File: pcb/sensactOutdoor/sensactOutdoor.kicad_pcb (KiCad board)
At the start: 2 copper layers, 100 x 81 mm, 126 parts, among them J1 48V, J10 CAN, J11 EXT2, J12 OW, J13 RGB, J14 CAN, J15 PWM_OUT, J16 24V, J2 Conn_01x03, J3 Conn_01x03, J4 PROG, J5 LED CC, J7 EXT1, J8 PWM_OUT, J9 230V, K1 ALDP105W, K2 ALDP105W, K3 ALDP105W, K4 ALDP105W, K5 ALDP105W, K6 ALDP105W, M1 BxxyyS-1WR, Q1 N, Q10 BC847, Q11 BC847, Q2 N, Q3 N, Q4 N, Q5 N, Q6 BC847, Q7 BC847, Q8 BC847, Q9 BC847, SW1 TERM OFF ON, SW2 RESET, U1 ESP32-WROOM-32U, U2 A6211, U3 LM2596Board, U4 ISO1050DUB, U5 AMS1117-3.3, U6 RF, U7 RX470B, U8 EL817

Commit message: Various PCB Updates
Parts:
- removed D7: LK1, LED_SMD:LED_0805_2012Metric_Pad1.15x1.40mm_HandSolder
- removed R34: k22, Resistor_SMD:R_0805_2012Metric_Pad1.20x1.40mm_HandSolder
- added D10: D, liebler_SEMICONDUCTORS:D_SOD-123_handsolder, B.Cu at (93.2, 25.1)
- added D11: D, liebler_SEMICONDUCTORS:D_SOD-123_handsolder, B.Cu at (93.1, 33.0)
- added D12: D, liebler_SEMICONDUCTORS:D_SOD-123_handsolder, B.Cu at (93.0, 45.2)
- added D13: D, liebler_SEMICONDUCTORS:D_SOD-123_handsolder, B.Cu at (93.0, 51.1)
- added D14: D, liebler_SEMICONDUCTORS:D_SOD-123_handsolder, B.Cu at (93.2, 59.1)
- added D15: D, liebler_SEMICONDUCTORS:D_SOD-123_handsolder, B.Cu at (93.2, 68.6)
- added U9: MAX98357_MODULE, Connector_PinHeader_2.54mm:PinHeader_1x07_P2.54mm_Vertical, F.Cu at (81.4, 43.3)
- moved R24 9.46 mm to (90.6, 56.8), turned to 270 degrees
- moved R5 7.53 mm to (84.6, 28.3)
- moved Q7 7.15 mm to (85.9, 34.2), turned to 270 degrees
- moved R23 5.81 mm to (87.2, 51.1), turned to 180 degrees
- moved Q10 5.39 mm to (86.6, 54.9), turned to 270 degrees
- moved R6 5.27 mm to (83.1, 33.5), turned to 270 degrees
- moved Q11 5.23 mm to (87.6, 60.5), turned to 270 degrees
- moved Q6 4.83 mm to (89.3, 27.6)
- moved R27 0.76 mm to (82.3, 61.7)
- moved C11 0.51 mm to (77.1, 58.2)
- moved C24 0.51 mm to (77.1, 60.6)
- moved C25 0.51 mm to (77.1, 63.1)
- moved D9 0.46 mm to (42.1, 33.0)
- moved U4 0.08 mm to (39.2, 65.5)
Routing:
- net +5V: track 155.0 -> 177.0 mm
- net +3V3: track 159.5 -> 170.8 mm, vias 3 -> 5
- net Net-(D12-Pad2): track 2.57 -> 13.4 mm
- net Net-(D14-Pad2): track 2.62 -> 12.0 mm
- net K1: track 28.2 -> 19.2 mm
- net Net-(D15-Pad2): track 2.88 -> 11.6 mm
- net Net-(D11-Pad2): track 2.99 -> 11.4 mm
- net Net-(D7-Pad2): track 8.22 -> 0.00 mm, vias 1 -> 0
- net Net-(D10-Pad2): track 1.87 -> 7.47 mm
- net K5: track 46.2 -> 41.3 mm
- net K2: track 22.2 -> 18.6 mm
- net Net-(Q11-Pad1): track 2.45 -> 4.60 mm
- net GND: track 117.5 -> 119.2 mm, vias 18 -> 17
- net SDA: track 28.5 -> 29.8 mm
- net K6: track 54.5 -> 53.3 mm
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
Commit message: Updated sensactHsNano
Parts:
- added JP3: 5Vx, Connector_PinHeader_2.54mm:PinHeader_1x02_P2.54mm_Vertical, F.Cu at (79.2, 69.9)
- D10, D11, D12, D13, D14, D15: value D -> 1N4148
- moved C5 21.1 mm to (61.1, 77.3), turned to 0 degrees
- moved C7 13.0 mm to (64.5, 66.5)
- moved C9 12.9 mm to (62.2, 66.5)
- moved C21 0.13 mm to (61.1, 74.9)
- moved C20 0.06 mm to (61.1, 72.6)
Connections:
- PS1 pad 4: +5V -> Net-(JP3-Pad1)
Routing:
- net +5V: track 177.0 -> 166.8 mm
- net Net-(JP3-Pad1): track 0.00 -> 4.66 mm
- net GND: track 119.2 -> 123.1 mm

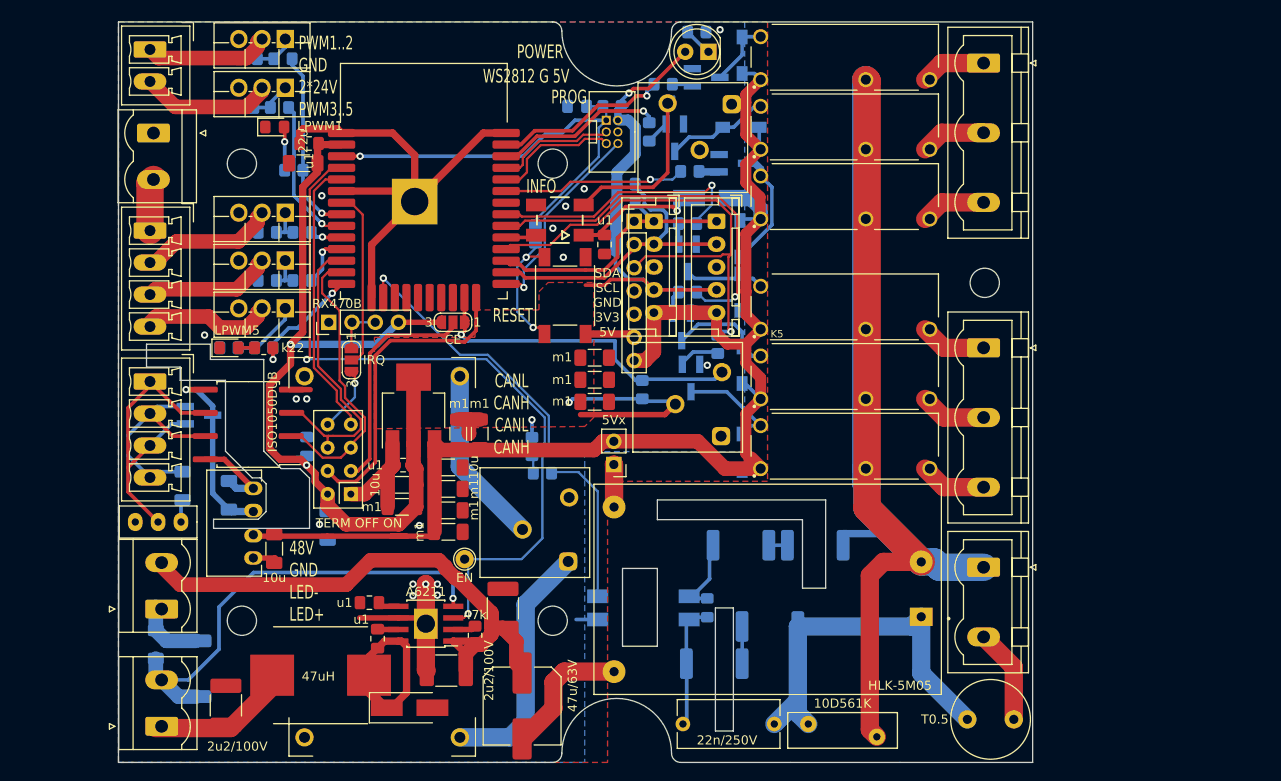
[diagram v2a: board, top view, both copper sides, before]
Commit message: sensactUP2, sensactHsNano sensactHsLED sensactOutdoor as ordered at JLCPCB
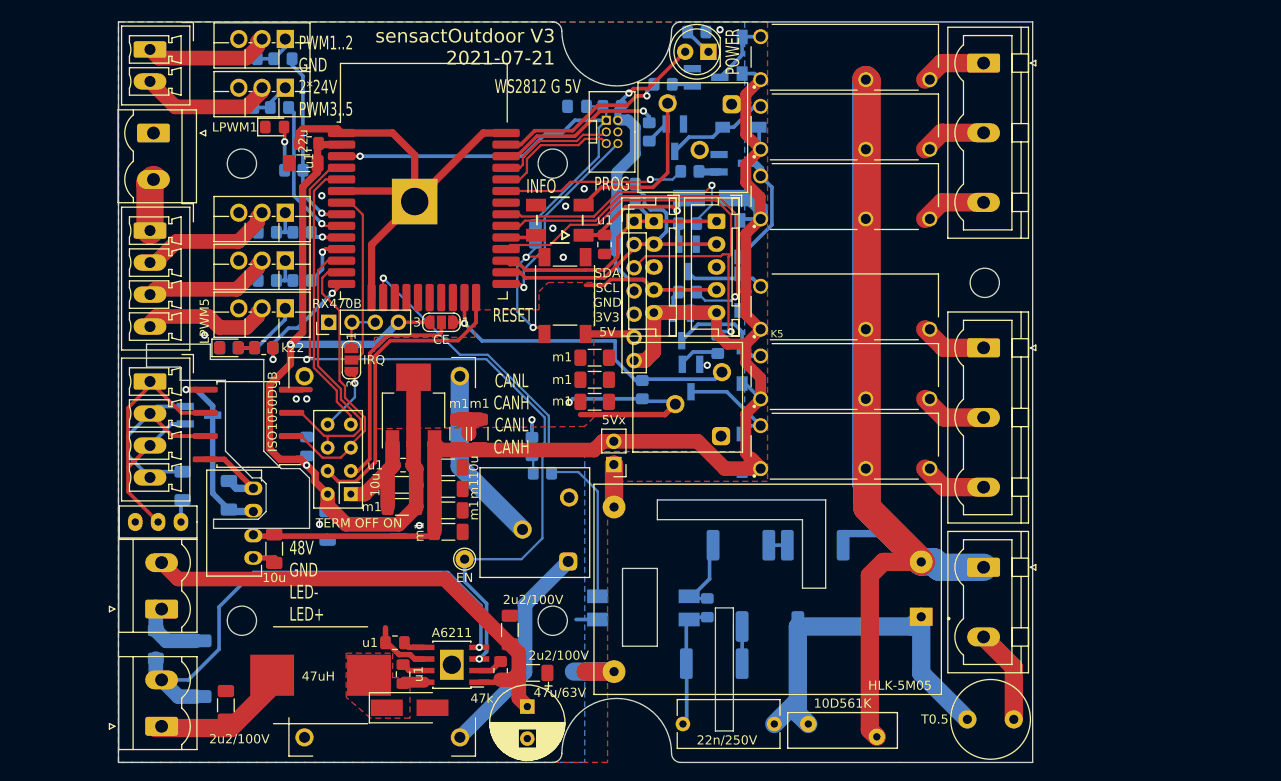
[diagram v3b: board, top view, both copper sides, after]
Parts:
- C1: footprint Capacitor_SMD:C_Elec_8x10.2 -> Capacitor_THT:CP_Radial_D8.0mm_P3.50mm
- C10, C2, C4: footprint Capacitor_SMD:C_1812_4532Metric_Pad1.57x3.40mm_HandSolder -> Capacitor_SMD:C_1206_3216Metric_Pad1.33x1.80mm_HandSolder
- moved C4 8.26 mm to (67.8, 88.0), turned to 90 degrees
- moved C2 7.80 mm to (70.4, 92.7), turned to 0 degrees
- moved U2 5.32 mm to (61.5, 91.8)
- moved C6 5.20 mm to (55.2, 89.4)
- moved C8 4.78 mm to (56.1, 92.8)
- moved R1 4.77 mm to (66.8, 92.5)
- moved JP1 1.27 mm to (60.3, 54.4)
- moved C1 0.58 mm to (69.7, 96.4)
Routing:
- net GND: track 123.1 -> 105.4 mm, vias 17 -> 12
- net /LED_SW: track 19.6 -> 2.40 mm
- net /LED_CC-: track 49.7 -> 55.8 mm
- net +48V: track 59.7 -> 54.2 mm
- net LED_CC_EN: track 57.6 -> 61.9 mm
- net /OUT+: track 27.4 -> 24.1 mm
- net +3V3: track 170.8 -> 169.5 mm
- net CE: track 25.0 -> 24.1 mm
- net CSN: track 34.1 -> 33.5 mm
- net OneWire: track 36.4 -> 37.0 mm
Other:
- board text added: "sensactOutdoor V3 2021-07-21"

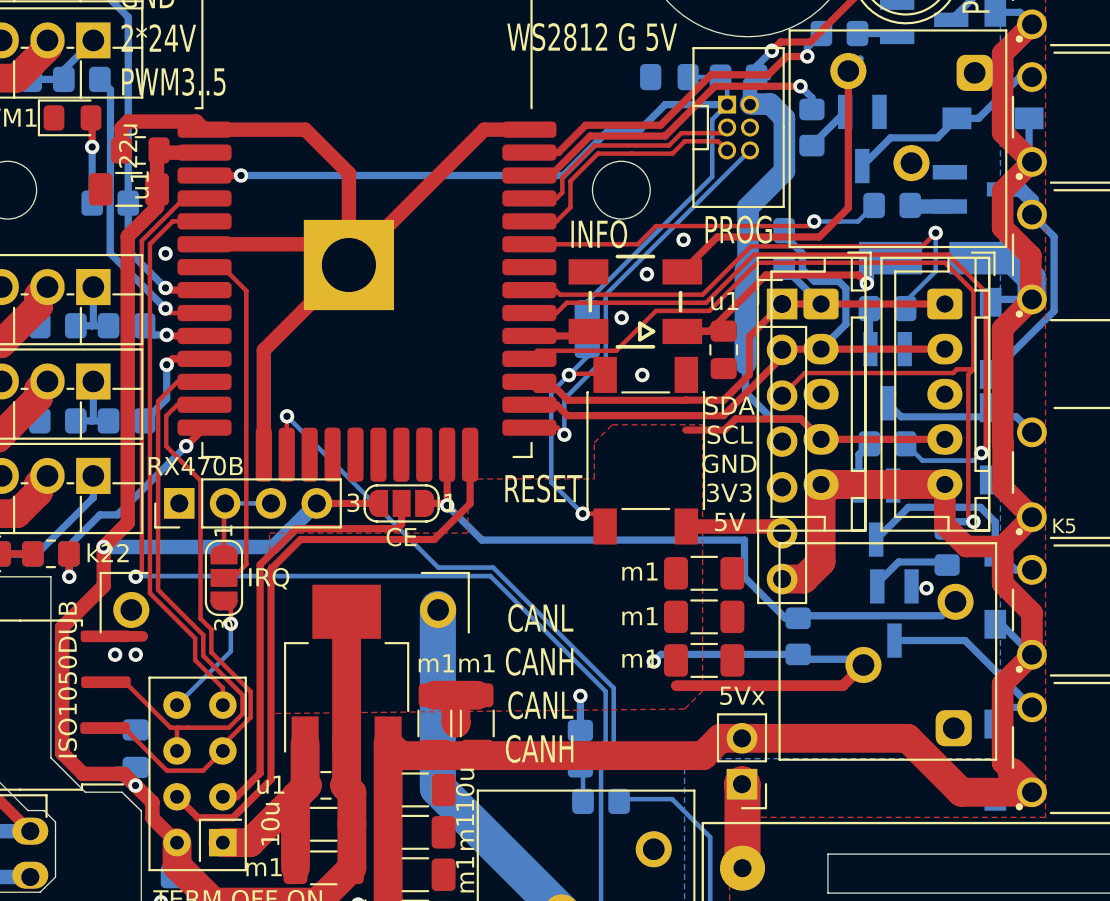
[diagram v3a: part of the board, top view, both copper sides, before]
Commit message: sensactHsNano for Reflow Soldering
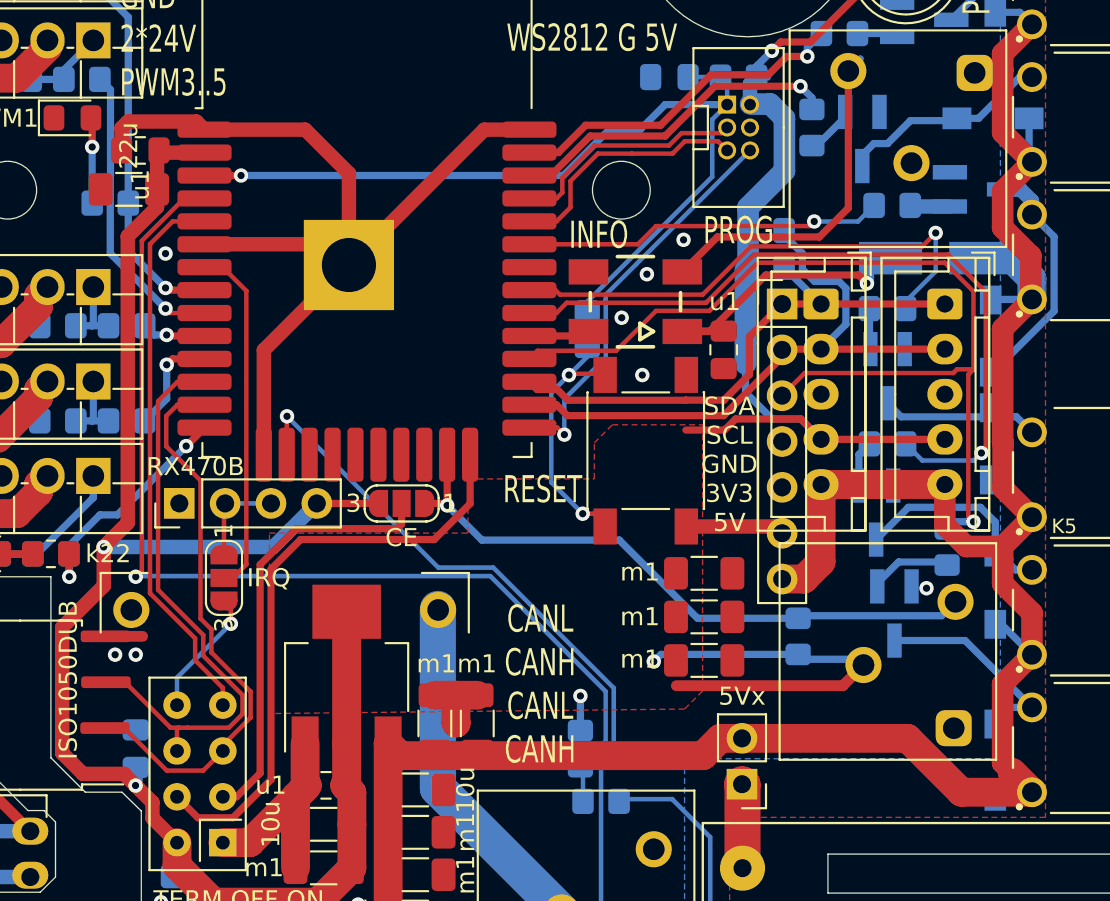
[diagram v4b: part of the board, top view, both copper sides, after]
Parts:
- moved D12 0.13 mm to (93.0, 45.1)
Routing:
- net OneWire: track 37.0 -> 35.8 mm

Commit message: Various
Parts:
- moved K6 35.8 mm to (139.8, 62.5)
- moved PS1 7.68 mm to (90.9, 77.8)
- moved K1 6.94 mm to (104.5, 32.3)
- moved K2 6.82 mm to (104.5, 39.8)
- moved K3 6.70 mm to (104.5, 47.3)
- moved RV1 5.90 mm to (100.2, 92.4)
- moved C23 5.80 mm to (96.7, 92.5)
- moved J9 5.26 mm to (114.7, 79.4)
- moved K4 2.13 mm to (104.5, 54.8)
- moved K5 2.01 mm to (104.5, 62.3)
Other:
- board size 100 x 81 mm -> 100 x 74.6 mm
- net class 230V removed
- net class 48V removed
- net class Default removed
- net class ISOLATED removed

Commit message: Various
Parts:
- removed C25: m1, Capacitor_SMD:C_1206_3216Metric_Pad1.33x1.80mm_HandSolder
- removed C26, C27: 10u, Capacitor_SMD:C_1206_3216Metric_Pad1.33x1.80mm_HandSolder
- removed J12: OW, liebler_CONN:KF250-3.5-3P-A
- removed J14: CAN, Connector_Phoenix_MC:PhoenixContact_MCV_1,5_4-G-3.5_1x04_P3.50mm_Vertical
- removed JP1: CE, Jumper:SolderJumper-3_P1.3mm_Open_RoundedPad1.0x1.5mm_NumberLabels
- removed JP2: IRQ, Jumper:SolderJumper-3_P1.3mm_Open_RoundedPad1.0x1.5mm_NumberLabels
- removed JP3: 5Vx, Connector_PinHeader_2.54mm:PinHeader_1x02_P2.54mm_Vertical
- removed L2: 47uH, liebler_PASSIVES:L_1040
- removed M1: BxxyyS-1WR, liebler_MODULES:BxxxxS-1W
- added D16: LPWM1, LED_SMD:LED_0603_1608Metric, F.Cu at (93.3, 50.5)
- added D17: LPWM1, LED_SMD:LED_0603_1608Metric, F.Cu at (93.3, 58.1)
- added D18: LPWM1, LED_SMD:LED_0603_1608Metric, F.Cu at (93.3, 65.7)
- added D19: LPWM2, LED_SMD:LED_0603_1608Metric, F.Cu at (34.3, 28.0)
- added D20: LPWM3, LED_SMD:LED_0603_1608Metric, F.Cu at (34.3, 47.9)
- added D21: LPWM4, LED_SMD:LED_0603_1608Metric, F.Cu at (34.3, 51.4)
- added D22: NUP2105, Package_TO_SOT_SMD:SOT-23_Handsoldering, B.Cu at (48.4, 59.6)
- added D7: Betrieb, LED_THT:LED_D5.0mm-4_RGB_Staggered_Pins, F.Cu at (71.8, 46.4)
- added J6: CAN BUS, Connector_Phoenix_MC:PhoenixContact_MCV_1,5_4-G-3.5_1x04_P3.50mm_Vertical, F.Cu at (48.7, 64.1)
- added L1: 47u, Inductor_SMD:L_Abracon_ASPI-0630LR, F.Cu at (45.8, 91.6)
- added R10: 1R, Resistor_SMD:R_0805_2012Metric, F.Cu at (38.7, 100.1)
- added R34: k47, Resistor_SMD:R_0402_1005Metric, F.Cu at (93.3, 33.1)
- added R37: k47, Resistor_SMD:R_0402_1005Metric, F.Cu at (93.3, 40.7)
- added R38: k47, Resistor_SMD:R_0402_1005Metric, F.Cu at (93.3, 53.0)
- added R39: k47, Resistor_SMD:R_0402_1005Metric, F.Cu at (93.3, 60.6)
- added R40: k47, Resistor_SMD:R_0402_1005Metric, F.Cu at (93.3, 68.2)
- added R41: k22, Resistor_SMD:R_0402_1005Metric, F.Cu at (34.3, 30.1)
- added R42: k22, Resistor_SMD:R_0402_1005Metric, F.Cu at (33.8, 45.4)
- added R43: k22, Resistor_SMD:R_0402_1005Metric, F.Cu at (34.8, 45.4)
- added R44: 4k7, Resistor_SMD:R_0805_2012Metric_Pad1.20x1.40mm_HandSolder, B.Cu at (43.6, 55.4)
- added R45: K12, Resistor_SMD:R_1206_3216Metric, F.Cu at (49.9, 81.9)
- added SW3: TERM ON->, liebler_MECH:Switch_SS12D00, F.Cu at (46.9, 81.9)
- added TH1: Thermistor_NTC, Capacitor_THT:C_Disc_D3.4mm_W2.1mm_P2.50mm, F.Cu at (45.0, 33.5)
- added TP1: 48V, TestPoint:TestPoint_THTPad_D2.0mm_Drill1.0mm, F.Cu at (35.2, 83.2)
- C1: value 47u/63V -> m1; footprint Capacitor_THT:CP_Radial_D8.0mm_P3.50mm -> Capacitor_SMD:C_1206_3216Metric
- C10: value 2u2/100V -> 1n/25V; footprint Capacitor_SMD:C_1206_3216Metric_Pad1.33x1.80mm_HandSolder -> Capacitor_SMD:C_0402_1005Metric
- C11, C9: value m1 -> u1; footprint Capacitor_SMD:C_1206_3216Metric_Pad1.33x1.80mm_HandSolder -> Capacitor_SMD:C_0402_1005Metric
- C12, C14, C17: footprint Capacitor_SMD:C_1206_3216Metric_Pad1.33x1.80mm_HandSolder -> Capacitor_SMD:C_0603_1608Metric
- C13, C16: footprint Capacitor_SMD:C_0805_2012Metric_Pad1.18x1.45mm_HandSolder -> Capacitor_SMD:C_0402_1005Metric
- C15: footprint Capacitor_SMD:C_0805_2012Metric_Pad1.18x1.45mm_HandSolder -> Capacitor_SMD:C_0402_1005Metric; moved to F.Cu
- C18: value u1 -> 1u/25V; footprint Capacitor_SMD:C_0805_2012Metric_Pad1.18x1.45mm_HandSolder -> Capacitor_SMD:C_1206_3216Metric; moved to F.Cu
- C19: value m1 -> 1u/50V; footprint Capacitor_SMD:C_1206_3216Metric_Pad1.33x1.80mm_HandSolder -> Capacitor_SMD:C_1206_3216Metric
- C2, C4: value 2u2/100V -> m1; footprint Capacitor_SMD:C_1206_3216Metric_Pad1.33x1.80mm_HandSolder -> Capacitor_SMD:C_1206_3216Metric
- C20, C5, C7: footprint Capacitor_SMD:C_1206_3216Metric_Pad1.33x1.80mm_HandSolder -> Capacitor_SMD:C_1206_3216Metric
- C21: value m1 -> 10u/100V; footprint Capacitor_SMD:C_1206_3216Metric_Pad1.33x1.80mm_HandSolder -> Capacitor_SMD:C_2220_5650Metric
- C22: footprint Capacitor_SMD:C_1206_3216Metric_Pad1.33x1.80mm_HandSolder -> Capacitor_SMD:C_0603_1608Metric; moved to F.Cu
- C24: value m1 -> u1; footprint Capacitor_SMD:C_1206_3216Metric_Pad1.33x1.80mm_HandSolder -> Capacitor_SMD:C_0805_2012Metric_Pad1.18x1.45mm_HandSolder; moved to B.Cu
- C3, C6, C8: value u1 -> m1; footprint Capacitor_SMD:C_0805_2012Metric_Pad1.18x1.45mm_HandSolder -> Capacitor_SMD:C_1206_3216Metric
- D10: value 1N4148 -> SM4007PL; footprint liebler_SEMICONDUCTORS:D_SOD-123_handsolder -> Diode_SMD:D_SOD-123F; moved to F.Cu
- D11: value 1N4148 -> Stellgröße; footprint liebler_SEMICONDUCTORS:D_SOD-123_handsolder -> LED_THT:LED_D5.0mm-4_RGB_Staggered_Pins; moved to F.Cu
- D12: value 1N4148 -> SS210; footprint liebler_SEMICONDUCTORS:D_SOD-123_handsolder -> liebler_SEMICONDUCTORS:D_SMA; moved to F.Cu
- D13, D14, D15: value 1N4148 -> LPWM1; footprint liebler_SEMICONDUCTORS:D_SOD-123_handsolder -> LED_SMD:LED_0603_1608Metric; moved to F.Cu
- D2: value D -> SM4007PL; footprint Diode_SMD:D_SMA_Handsoldering -> Diode_SMD:D_SOD-123F
- D3: value POWER -> SM4007PL; footprint LED_THT:LED_D5.0mm -> Diode_SMD:D_SOD-123F
- D4: value D -> SM4007PL; footprint Diode_SMD:D_SMA_Handsoldering -> Diode_SMD:D_SOD-123F; moved to F.Cu
- D5: value INFO -> SM4007PL; footprint liebler_SEMICONDUCTORS:WS2812b_handsolder -> Diode_SMD:D_SOD-123F
- D6: value NUP2105L -> SM4007PL; footprint Package_TO_SOT_SMD:SOT-23_Handsoldering -> Diode_SMD:D_SOD-123F; moved to F.Cu
- D8, D9: footprint LED_SMD:LED_0805_2012Metric_Pad1.15x1.40mm_HandSolder -> LED_SMD:LED_0603_1608Metric
- J10: value CAN -> LED_EXT
- Q10, Q11, Q6, Q7, Q8, Q9: footprint Package_TO_SOT_SMD:SOT-23_Handsoldering -> Package_TO_SOT_SMD:SOT-23; moved to F.Cu
- R1: value 47k -> 10k; footprint Resistor_SMD:R_0805_2012Metric_Pad1.20x1.40mm_HandSolder -> Resistor_SMD:R_0402_1005Metric
- R11, R12, R14, R15, R17, R18, R19, R20, R21, R22, R23, R24, R25, R26, R29, R3, R32, R36, R5, R6, R7, R8, R9: footprint Resistor_SMD:R_0805_2012Metric_Pad1.20x1.40mm_HandSolder -> Resistor_SMD:R_0402_1005Metric; moved to F.Cu
- R13: value k22 -> 1R; footprint Resistor_SMD:R_0805_2012Metric_Pad1.20x1.40mm_HandSolder -> Resistor_SMD:R_0805_2012Metric; moved to F.Cu
- R2: value R300 -> 10k; footprint Resistor_SMD:R_1206_3216Metric_Pad1.30x1.75mm_HandSolder -> Resistor_SMD:R_0402_1005Metric; moved to F.Cu
- R27: value 4k7 -> 2R2; footprint Resistor_SMD:R_0805_2012Metric_Pad1.20x1.40mm_HandSolder -> Resistor_SMD:R_0805_2012Metric; moved to F.Cu
- R33: value 120R -> k47; footprint Resistor_SMD:R_1206_3216Metric_Pad1.30x1.75mm_HandSolder -> Resistor_SMD:R_0402_1005Metric; moved to F.Cu
- R35: footprint Resistor_SMD:R_0805_2012Metric_Pad1.20x1.40mm_HandSolder -> Resistor_SMD:R_0402_1005Metric
- R4: value Rxxx -> 1R; footprint Resistor_SMD:R_2512_6332Metric_Pad1.40x3.35mm_HandSolder -> Resistor_SMD:R_0805_2012Metric; moved to F.Cu
- SW1: value TERM OFF ON -> SW_SPDT; footprint liebler_MECH:SS12D00 -> liebler_MECH:Switch_SS12D00
- SW2: footprint liebler_MECH:SW_Push_1P1T_NO_6x6mm_H9.5mm -> Button_Switch_THT:SW_PUSH_6mm_H13mm
- U1: footprint smopla:ESP32-WROOM-32_HANDSOLDER -> RF_Module:ESP32-WROOM-32U
- U2: value A6211 -> BP1808; footprint sensact:SOIC-8_3.9x4.9mm_Pitch1.27mm_pad_handsolder -> Package_SO:SOIC-8-1EP_3.9x4.9mm_P1.27mm_EP2.41x3.3mm_ThermalVias
- U4: value ISO1050DUB -> SN65HVD230; footprint liebler_SEMICONDUCTORS:SOP-8_6.62x9.15mm_P2.54mm_handsolder -> liebler_SEMICONDUCTORS:SOIC-8_3.9x4.9mm_Pitch1.27mm_handsolder; moved to B.Cu
- U5: footprint smopla:SOT-223-3_TabPin2_HANDSOLDER -> Package_TO_SOT_SMD:SOT-223-3_TabPin2
- U6: footprint RF_Module:nRF24L01_Breakout -> liebler_MODULES:nRF24L01_Breakout
- U7: value RX470B -> DCDC_MP2315; footprint Connector_PinHeader_2.54mm:PinHeader_1x04_P2.54mm_Vertical -> liebler_MODULES:DCDC_MP2315
- moved R13 94.2 mm to (34.7, 100.1), turned to -90 degrees
- moved R33 77.0 mm to (93.3, 25.6), turned to 90 degrees
- moved D2 73.4 mm to (91.4, 31.8), turned to 90 degrees
- moved D12 67.3 mm to (50.7, 97.5), turned to 90 degrees
- moved R1 62.0 mm to (46.7, 33.8), turned to 90 degrees
- moved R27 59.6 mm to (36.7, 100.1), turned to -90 degrees
- moved D6 58.0 mm to (91.8, 62.9), turned to 180 degrees
- moved SW1 50.7 mm to (79.2, 67.3), turned to 90 degrees
- moved C3 39.1 mm to (60.5, 80.7), turned to 0 degrees
- moved K6 35.7 mm to (104.5, 67.9)
- moved J13 35.2 mm to (60.5, 46.0)
- moved D11 35.1 mm to (71.8, 61.0), turned to 90 degrees
- moved C24 31.6 mm to (48.4, 47.3)
- moved R29 31.5 mm to (51.2, 42.9), turned to 0 degrees
- moved R9 31.1 mm to (48.2, 26.4), turned to 90 degrees
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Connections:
- C1 pad 1: +48V -> +5V
- C10 pad 1: /LED_CC -> /COMP
- C11 pad 1: +3V3 -> GND
- C11 pad 2: GND -> +5V
- C15 pad 1: GND -> PROG_EN
- C15 pad 2: PROG_EN -> GND
- C18 pad 1: +3V3 -> Net-(C18-Pad1)
- C19 pad 1: +3V3 -> /LED-
- C19 pad 2: GND -> +48V
- C2 pad 1: +48V -> +3V3
- C21 pad 1: +5V -> +48V
- C24 pad 1: +3V3 -> GND
- C24 pad 2: GND -> +3V3
- C3 pad 1: GND -> +5V
- C3 pad 2: Net-(C3-Pad2) -> GND
- C4 pad 1: +48V -> +5V
- C6 pad 1: Net-(C6-Pad1) -> +3V3
- C7 pad 1: +5V -> +3V3
- C8 pad 1: /LED_SW -> +3V3
- C8 pad 2: Net-(C8-Pad2) -> GND
- C9 pad 1: +5V -> GND
- C9 pad 2: GND -> +5V
- D11 pad 1: +5V -> Net-(D11-Pad1)
- D11 pad 2: Net-(D11-Pad2) -> GND
- D12 pad 1: +5V -> +48V
- D12 pad 2: Net-(D12-Pad2) -> /SW
- D13 pad 1: +5V -> Net-(D10-Pad2)
- D14 pad 1: +5V -> Net-(D14-Pad1)
- D15 pad 1: +5V -> Net-(D15-Pad1)
- D2 pad 1: /LED_SW -> +5V
- D2 pad 2: GND -> Net-(D14-Pad1)
- D3 pad 1: Net-(D3-Pad1) -> +5V
- D3 pad 2: +3V3 -> Net-(D15-Pad1)
- D4 pad 1: Net-(C3-Pad2) -> +5V
- D4 pad 2: +5V -> Net-(D16-Pad1)
- D5 pad 1: Net-(C3-Pad2) -> +5V
- D5 pad 2: Net-(D5-Pad2) -> Net-(D17-Pad1)
- D6 pad 1: CANL -> +5V
- D6 pad 2: CANH -> Net-(D18-Pad1)
- J13 pad 2: GND -> Net-(D11-Pad1)
- J13 pad 3: Net-(D5-Pad2) -> GND
- J5 pad 1: /LED_CC -> /LED+
- J5 pad 2: /LED_CC- -> /LED-
- K2 pad A2: Net-(D11-Pad2) -> Net-(D14-Pad1)
- K3 pad A2: Net-(D12-Pad2) -> Net-(D15-Pad1)
- K4 pad A2: Net-(D13-Pad2) -> Net-(D16-Pad1)
- K5 pad A2: Net-(D14-Pad2) -> Net-(D17-Pad1)
- K6 pad A2: Net-(D15-Pad2) -> Net-(D18-Pad1)
- PS1 pad 4: Net-(JP3-Pad1) -> Net-(PS1-Pad4)
- Q10 pad 3: Net-(D14-Pad2) -> Net-(D17-Pad1)
- Q11 pad 3: Net-(D15-Pad2) -> Net-(D18-Pad1)
- Q7 pad 3: Net-(D11-Pad2) -> Net-(D14-Pad1)
- Q8 pad 3: Net-(D12-Pad2) -> Net-(D15-Pad1)
- Q9 pad 3: Net-(D13-Pad2) -> Net-(D16-Pad1)
- R1 pad 1: Net-(R1-Pad1) -> +3V3
- R1 pad 2: +48V -> THERM
- R11 pad 1: PWM5 -> CAN_TX
- R13 pad 1: Net-(D3-Pad1) -> /LED+
- R13 pad 2: GND -> +48V
- R2 pad 1: /LED_CC- -> LED_CC_EN
- R27 pad 1: +3V3 -> /LED+
- R27 pad 2: OneWire -> +48V
- R29 pad 1: MAINS -> CAN_RX
- R32 pad 2: MAINS -> CAN_RX
- R33 pad 1: CANH -> +5V
- R33 pad 2: Net-(R33-Pad2) -> Net-(D13-Pad2)
- R35 pad 1: PWM5 -> CAN_TX
- R4 pad 1: /LED_CC- -> /LED+
- R4 pad 2: GND -> +48V
- SW1 pad 1: Net-(R33-Pad2) -> Net-(PS1-Pad4)
- SW1 pad 2: CANL -> +5V
- SW1 pad 3: Net-(SW1-Pad3) -> unconnected-(SW1-Pad3)
- U1 pad 12: CANT -> MOSI
- U1 pad 13: CANR -> SCK
- U1 pad 14: PWM5 -> CAN_TX
- U1 pad 17: Net-(U1-Pad17) -> unconnected-(U1-Pad17)
- U1 pad 18: Net-(U1-Pad18) -> unconnected-(U1-Pad18)
- U1 pad 19: Net-(U1-Pad19) -> unconnected-(U1-Pad19)
- U1 pad 20: Net-(U1-Pad20) -> unconnected-(U1-Pad20)
- U1 pad 21: Net-(U1-Pad21) -> unconnected-(U1-Pad21)
- U1 pad 22: Net-(U1-Pad22) -> unconnected-(U1-Pad22)
- U1 pad 23: OneWire -> CE
- U1 pad 29: SIGNAL -> RGB_LED
- U1 pad 32: Net-(U1-Pad32) -> unconnected-(U1-Pad32)
- U1 pad 4: MAINS -> CAN_RX
- U1 pad 5: MISO -> IRQ
- U1 pad 6: GND -> MISO
- U1 pad 7: IRQ -> THERM
- U2 pad 1: +48V -> unconnected-(U2-Pad1)
- U2 pad 2: Net-(R1-Pad1) -> /COMP
- U2 pad 4: /LED_CC- -> GND
- U2 pad 5: Net-(C6-Pad1) -> /SW
- U2 pad 6: GND -> Net-(C18-Pad1)
- U2 pad 7: Net-(C8-Pad2) -> +48V
- U2 pad 8: /LED_SW -> /LED+
- U4 pad 1: +3V3 -> CAN_TX
- U4 pad 2: CANR -> GND
- U4 pad 3: CANT -> +3V3
- U4 pad 4: GND -> CAN_RX
- U4 pad 5: GND1 -> unconnected-(U4-Pad5)
- U4 pad 8: +5P -> Net-(R44-Pad1)
- U6 pad 5: CANR -> SCK
- U6 pad 6: CANT -> MOSI
- U6 pad 8: IRQ2 -> IRQ
- U7 pad 1: GND -> +5V
- U7 pad 2: IRQ1 -> GND
- U7 pad 3: IRQ1 -> +28V
- U7 pad 4: +3V3 -> unconnected-(U7-Pad4)
- U9 pad 4: Net-(U9-Pad4) -> unconnected-(U9-Pad4)
- U9 pad 5: Net-(U9-Pad5) -> unconnected-(U9-Pad5)
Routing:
- net CAN_RX: track 0.00 -> 83.3 mm, vias 0 -> 3
- net GND: track 105.4 -> 24.9 mm, vias 12 -> 44
- net +5V: track 166.8 -> 244.2 mm, vias 0 -> 1
- net MAINS: track 58.5 -> 0.00 mm, vias 1 -> 0
- net /LED_CC-: track 55.8 -> 0.00 mm, vias 1 -> 0
- net OneWire: track 35.8 -> 0.00 mm, vias 1 -> 0
- net MOSI: track 0.00 -> 34.4 mm
- net CANT: track 32.6 -> 0.00 mm
- net /LED+: track 0.00 -> 31.7 mm, vias 0 -> 2
- net CANR: track 31.5 -> 0.00 mm
- net SCK: track 0.00 -> 31.0 mm
- net CAN_TX: track 0.00 -> 29.7 mm, vias 0 -> 3
- net +3V3: track 169.1 -> 142.6 mm, vias 5 -> 6
- net Net-(D11-Pad1): track 0.00 -> 20.8 mm
- net PWM3: track 3.55 -> 24.3 mm, vias 1 -> 2
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- added copper zone on F.Cu, net /SW
- removed copper zone on F.Cu, net /LED_SW
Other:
- board size 100 x 74.6 mm -> 100 x 81 mm
- board text added: "5V from PSU 5V from Prog"
- board text added: "CANH"
- board text added: "CANL"
- board text added: "CANL CANH GND 24V"
- board text added: "GND RGB 5V"
- board text added: "INFO"
- board text added: "LED- LED+"
- board text added: "Out+ In+ Gnd"
- board text added: "PWM1 PWM2 GND 24V 24V PWM3 PWM4 PWM5 48V GND"
- board text added: "RESET"
- board text added: "STATUS"
- board text added: "TERM Off TERM On"
- board text added: "sensactOutdoor V4 2022-08-02"
- board text removed: "48V GND LED- LED+"
- board text removed: "CANL CANH CANL CANH"
- board text removed: "H"
- board text removed: "PWM1..2 GND 2*24V PWM3..5"
- board text removed: "WS2812 G 5V"
- board text removed: "sensactOutdoor V3 2021-07-21"
